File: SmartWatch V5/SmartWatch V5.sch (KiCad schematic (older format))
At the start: 60 parts, among them J1 10118192-0001LF, J10 TestPad, J2 , J7 TestPad, J8 TestPad, J9 TestPad, Q1 FDN340P, Q2 MMBT3904, Q3 MMBT3904, SW1 EVQ-P7J01P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

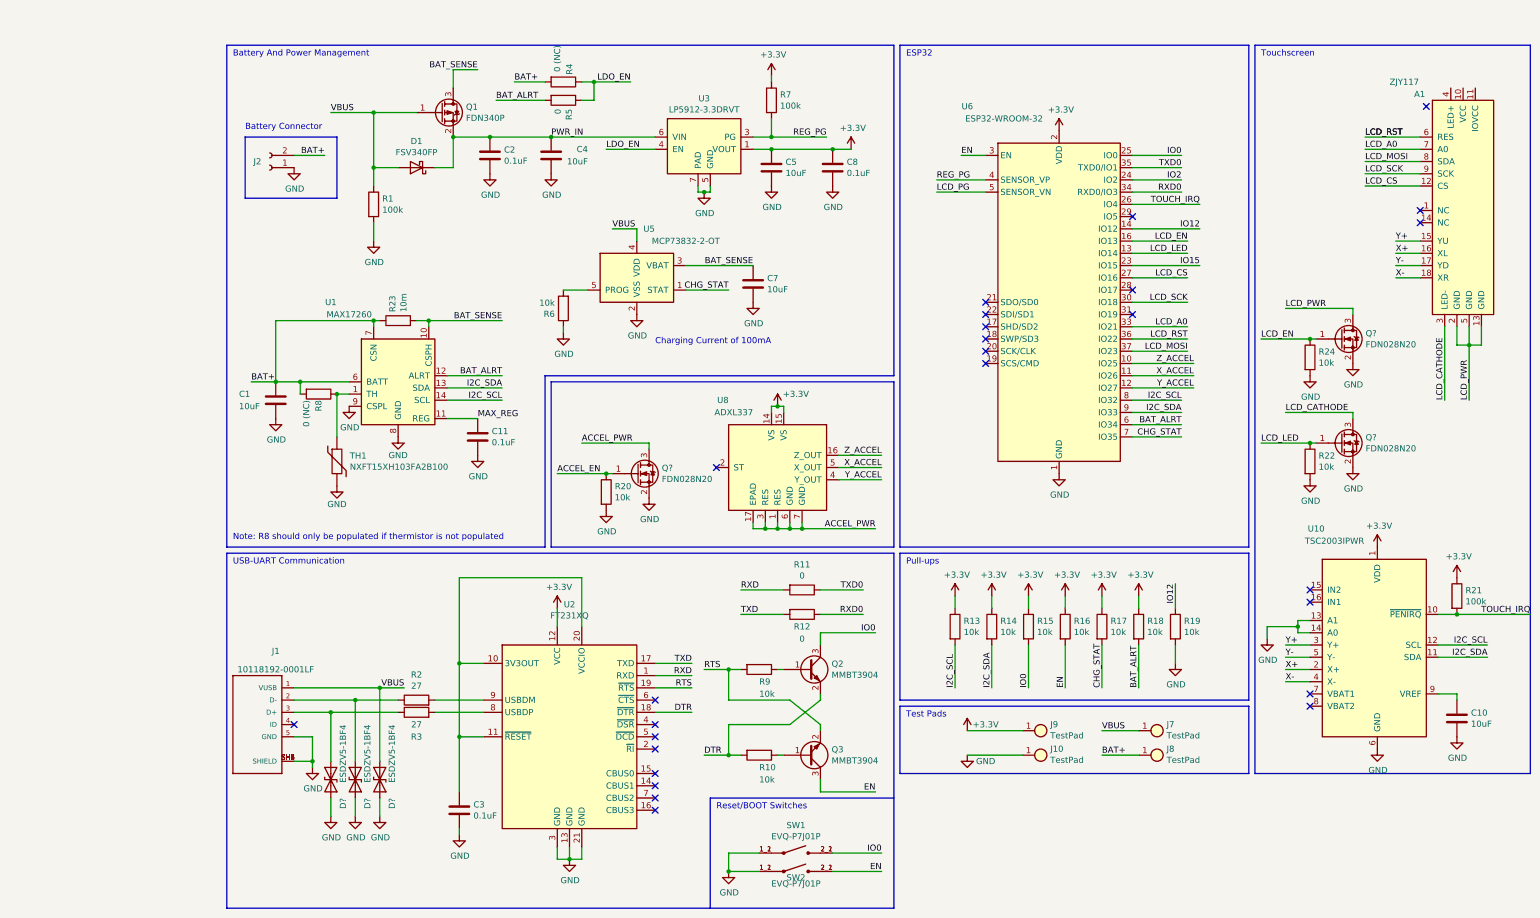
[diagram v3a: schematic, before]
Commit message: Added footprint for Thermistor
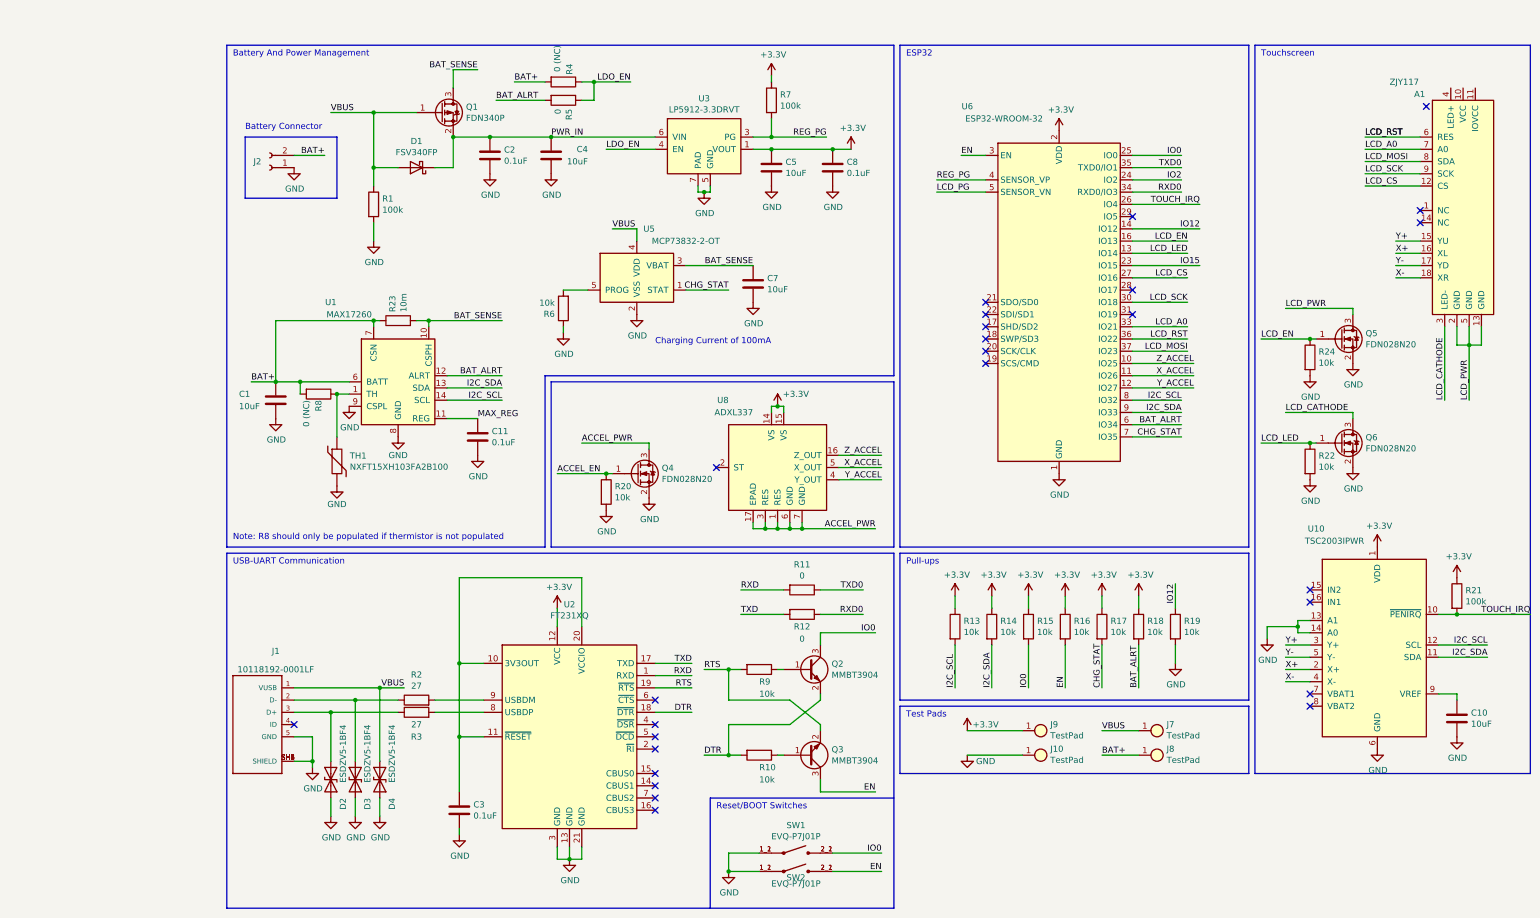
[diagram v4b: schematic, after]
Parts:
- TH1: footprint (none) -> Connector_PinHeader_1.00mm:PinHeader_1x02_P1.00mm_Vertical
- gave numbers to parts that had none: 6
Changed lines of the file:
@@
 F 0 "TH1" H 1555 3996 50  0000 L CNN
 F 1 "NXFT15XH103FA2B100" H 1555 3905 50  0000 L CNN
-F 2 "" H 1450 3950 50  0001 C CNN
+F 2 "Connector_PinHeader_1.00mm:PinHeader_1x02_P1.00mm_Vertical" H 1450 3950 50  0001 C CNN
 F 3 "https://www.murata.com/~/media/webrenewal/support/library/catalog/products/thermistor/ntc/r44e.ashx?la=en-us" H 1450 3950 50  0001 C CNN
 F 4 "490-5630-ND" H 1450 3950 50  0001 C CNN "digikey"
@@
 	3200 3300 6000 3300
 $Comp
-L Device:Q_NMOS_GSD Q?
+L Device:Q_NMOS_GSD Q6
 U 1 1 5F89B605
 P 9650 3800
-F 0 "Q?" H 9854 3846 50  0000 L CNN
+F 0 "Q6" H 9854 3846 50  0000 L CNN
 F 1 "FDN028N20" H 9854 3755 50  0000 L CNN
 F 2 "Package_TO_SOT_SMD:SOT-23" H 9850 3900 50  0001 C CNN
@@
 $EndComp
 $Comp
-L Device:Q_NMOS_GSD Q?
+L Device:Q_NMOS_GSD Q5
 U 1 1 5F89CF73
 P 9650 2950
-F 0 "Q?" H 9854 2996 50  0000 L CNN
+F 0 "Q5" H 9854 2996 50  0000 L CNN
 F 1 "FDN028N20" H 9854 2905 50  0000 L CNN
 F 2 "Package_TO_SOT_SMD:SOT-23" H 9850 3050 50  0001 C CNN
@@
 $EndComp
 $Comp
-L Device:Q_NMOS_GSD Q?
+L Device:Q_NMOS_GSD Q4
 U 1 1 5F89D454
 P 3900 4050
-F 0 "Q?" H 4104 4096 50  0000 L CNN
+F 0 "Q4" H 4104 4096 50  0000 L CNN
 F 1 "FDN028N20" H 4104 4005 50  0000 L CNN
 F 2 "Package_TO_SOT_SMD:SOT-23" H 4100 4150 50  0001 C CNN
@@
 	8950 550  8950 6500
 $Comp
-L Device:D_TVS D?
+L Device:D_TVS D2
 U 1 1 5F8FA488
 P 1400 6550
-F 0 "D?" H 1550 6650 50  0000 L CNN
+F 0 "D2" H 1550 6650 50  0000 L CNN
 F 1 "ESDZV5-1BF4" H 950 6650 50  0000 L CNN
 F 2 "Diode_SMD:D_0201_0603Metric" H 1400 6550 50  0001 C CNN
@@
 	1100 6000 1400 6000
 $Comp
-L Device:D_TVS D?
+L Device:D_TVS D3
 U 1 1 5F945157
 P 1600 6550
-F 0 "D?" H 1750 6650 50  0000 L CNN
+F 0 "D3" H 1750 6650 50  0000 L CNN
 F 1 "ESDZV5-1BF4" H 1150 6650 50  0000 L CNN
 F 2 "Diode_SMD:D_0201_0603Metric" H 1600 6550 50  0001 C CNN
@@
 $EndComp
 $Comp
-L power:GND #PWR?
+L power:GND #PWR0125
 U 1 1 5F945F46
 P 1400 6850
-F 0 "#PWR?" H 1400 6600 50  0001 C CNN
+F 0 "#PWR0125" H 1400 6600 50  0001 C CNN
 F 1 "GND" H 1405 6677 50  0000 C CNN
 F 2 "" H 1400 6850 50  0001 C CNN
@@
 $EndComp
 $Comp
-L power:GND #PWR?
+L power:GND #PWR0126
 U 1 1 5F946231
 P 1600 6850
-F 0 "#PWR?" H 1600 6600 50  0001 C CNN
+F 0 "#PWR0126" H 1600 6600 50  0001 C CNN
 F 1 "GND" H 1605 6677 50  0000 C CNN
 F 2 "" H 1600 6850 50  0001 C CNN
@@
 	1100 5900 1600 5900
 $Comp
-L Device:D_TVS D?
+L Device:D_TVS D4
 U 1 1 5FA53832
 P 1800 6550
-F 0 "D?" H 1950 6650 50  0000 L CNN
+F 0 "D4" H 1950 6650 50  0000 L CNN
 F 1 "ESDZV5-1BF4" H 1350 6650 50  0000 L CNN
 F 2 "Diode_SMD:D_0201_0603Metric" H 1800 6550 50  0001 C CNN
@@
 $EndComp
 $Comp
-L power:GND #PWR?
+L power:GND #PWR0127
 U 1 1 5FA53838
 P 1800 6850
-F 0 "#PWR?" H 1800 6600 50  0001 C CNN
+F 0 "#PWR0127" H 1800 6600 50  0001 C CNN
 F 1 "GND" H 1805 6677 50  0000 C CNN
 F 2 "" H 1800 6850 50  0001 C CNN

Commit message: Began 4 Layer Layout
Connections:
- net +3V3: now also A1.10 (VCC), A1.11 (IOVCC), A1.4 (LED+)
- net IO15: no longer names the net of U6.23 (IO15)
- net IO2: no longer names the net of U6.24 (IO2)
- net LCD_PG: no longer names the net of U6.5 (SENSOR_VN)
- no-connect marks 26 -> 29
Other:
- note added: "Selected Battery - https://www.digikey.com/product-detail/en/adafruit-industries-llc/3898/1528-2731-ND/9685336 (digikey part number: 1528-2731-ND)"
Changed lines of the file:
@@
 Text Label 3650 1400 0    50   ~ 0
 LDO_EN
-Text Label 6350 1750 0    50   ~ 0
-LCD_PG
-Wire Wire Line
-	6350 1750 6750 1750
 Wire Wire Line
 	4400 1750 4400 1700
@@
 Text Label 8500 1850 2    50   ~ 0
 TOUCH_IRQ
-Text Label 8350 1650 2    50   ~ 0
-IO2
 $Comp
 L Device:R R19
@@
 Wire Wire Line
 	8300 5600 8300 5450
-Wire Wire Line
-	7950 1650 8350 1650
 Wire Bus Line
 	8900 4650 8900 550
@@
 Wire Bus Line
 	11200 550  11200 6500
-Text Label 8500 2350 2    50   ~ 0
-IO15
 $Comp
 L CustomParts:TSC2003IPWR U10
@@
 Wire Bus Line
 	550  4700 550  7600
-Wire Wire Line
-	7950 2350 8500 2350
 Text Label 2900 850  0    50   ~ 0
 BAT+
-Text Label 10100 2150 0    50   ~ 0
-Y+
-Wire Wire Line
-	10100 2150 10300 2150
-Text Label 10100 2250 0    50   ~ 0
-X+
-Wire Wire Line
-	10100 2250 10300 2250
-Text Label 10100 2350 0    50   ~ 0
-Y-
-Wire Wire Line
-	10100 2350 10300 2350
-Text Label 10100 2450 0    50   ~ 0
-X-
-Wire Wire Line
-	10100 2450 10300 2450
 Wire Wire Line
 	8400 2450 7950 2450
@@
 Wire Wire Line
 	7950 2150 8400 2150
-NoConn ~ 10350 1050
 Wire Wire Line
 	10500 2850 10500 3450
@@
 Wire Wire Line
 	1800 5800 2000 5800
+Wire Wire Line
+	10100 2450 10300 2450
+Text Label 10100 2450 0    50   ~ 0
+X-
+Wire Wire Line
+	10100 2350 10300 2350
+Text Label 10100 2350 0    50   ~ 0
+Y-
+Wire Wire Line
+	10100 2250 10300 2250
+Text Label 10100 2250 0    50   ~ 0
+X+
+Wire Wire Line
+	10100 2150 10300 2150
+Text Label 10100 2150 0    50   ~ 0
+Y+
+NoConn ~ 7950 2350
+NoConn ~ 7950 1650
+$Comp
+L power:+3.3V #PWR0128
+U 1 1 5FB2118B
+P 10650 800
+F 0 "#PWR0128" H 10650 650 50  0001 C CNN
+F 1 "+3.3V" H 10665 973 50  0000 C CNN
+F 2 "" H 10650 800 50  0001 C CNN
+F 3 "" H 10650 800 50  0001 C CNN
+	1    10650 800
+	1    0    0    -1
+$EndComp
+Wire Wire Line
+	10550 900  10550 800
+Wire Wire Line
+	10550 800  10650 800
+Wire Wire Line
+	10750 800  10750 900
+Connection ~ 10650 800
+Wire Wire Line
+	10650 800  10750 800
+Wire Wire Line
+	10650 900  10650 800
+NoConn ~ 6750 1750
+NoConn ~ -1200 1350
+Text Notes 600  350  0    50   ~ 0
+Selected Battery - https://www.digikey.com/product-detail/en/adafruit-industries-llc/3898/1528-2731-ND/9685336 (digikey part number: 1528-2731-ND)
 $EndSCHEMATC

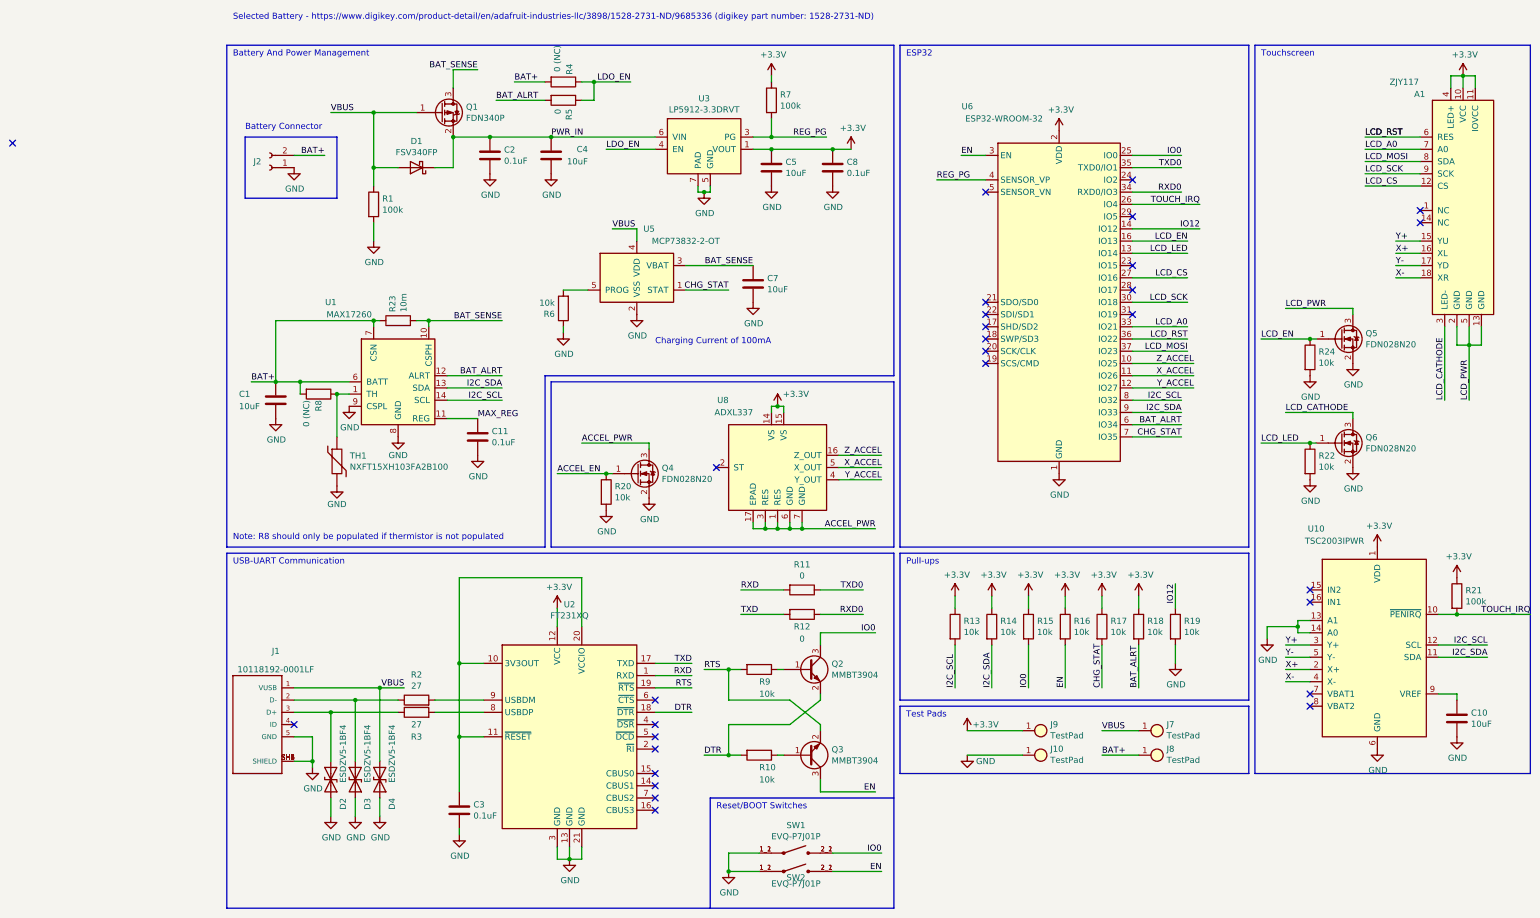
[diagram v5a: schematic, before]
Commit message: Removed 0 ohm jumpers on UART connection
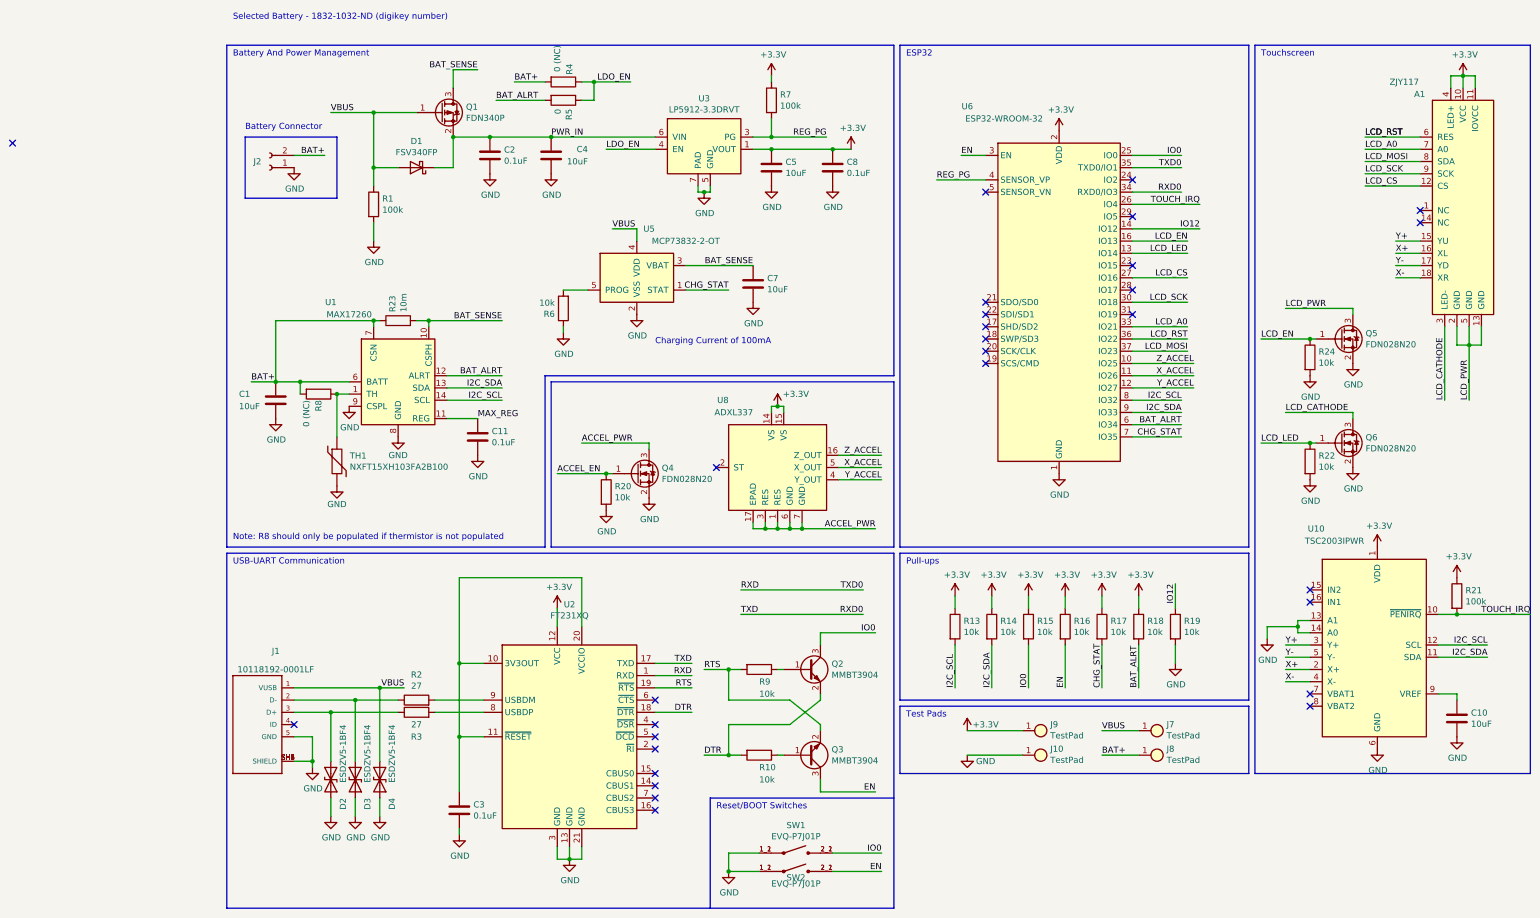
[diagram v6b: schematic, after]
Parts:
- removed R11, R12: 0, Resistor_SMD:R_0603_1608Metric, symbol Device:R
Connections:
- net TXD is gone; now on net RXD0: U2.17 (TXD)
- net TXD0 is gone; now on net RXD: U6.35 (TXD0/IO1)
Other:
- note added: "Selected Battery - 1832-1032-ND (digikey number)"
- note removed: "Selected Battery - https://www.digikey.com/product-detail/en/adafruit-industries-llc/3898/1528-2731-ND/9685336 (digikey part number: 1528-2731-ND)"
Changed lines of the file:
@@
 NoConn ~ 6750 3050
 NoConn ~ 6750 3150
-$Comp
-L Device:R R11
-U 1 1 5E6E7602
-P 5250 5000
-F 0 "R11" V 5043 5000 50  0000 C CNN
-F 1 "0" V 5134 5000 50  0000 C CNN
-F 2 "Resistor_SMD:R_0603_1608Metric" V 5180 5000 50  0001 C CNN
-F 3 "~" H 5250 5000 50  0001 C CNN
-F 4 "RMCF0805ZT0R00CT-ND" V 5250 5000 50  0001 C CNN "digikey"
-	1    5250 5000
-	0    1    1    0
-$EndComp
-$Comp
-L Device:R R12
-U 1 1 5E6E7B1F
-P 5250 5200
-F 0 "R12" V 5350 5200 50  0000 C CNN
-F 1 "0" V 5450 5200 50  0000 C CNN
-F 2 "Resistor_SMD:R_0603_1608Metric" V 5180 5200 50  0001 C CNN
-F 3 "~" H 5250 5200 50  0001 C CNN
-F 4 "RMCF0805ZT0R00CT-ND" V 5250 5200 50  0001 C CNN "digikey"
-	1    5250 5200
-	0    1    1    0
-$EndComp
-Wire Wire Line
-	4750 5000 5100 5000
-Wire Wire Line
-	4750 5200 5100 5200
-Wire Wire Line
-	5400 5200 5750 5200
-Wire Wire Line
-	5400 5000 5750 5000
 Text Label 4750 5000 0    50   ~ 0
 RXD
@@
 NoConn ~ -1200 1350
 Text Notes 600  350  0    50   ~ 0
-Selected Battery - https://www.digikey.com/product-detail/en/adafruit-industries-llc/3898/1528-2731-ND/9685336 (digikey part number: 1528-2731-ND)
+Selected Battery - 1832-1032-ND (digikey number)
+Wire Wire Line
+	4750 5000 5750 5000
+Wire Wire Line
+	4750 5200 5750 5200
 $EndSCHEMATC

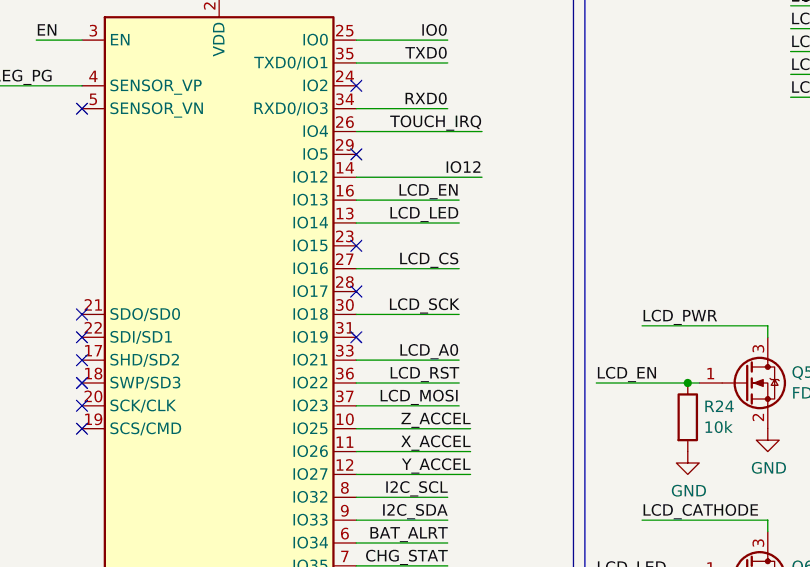
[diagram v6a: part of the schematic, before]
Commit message: Connected ACCEL_EN to ESP32
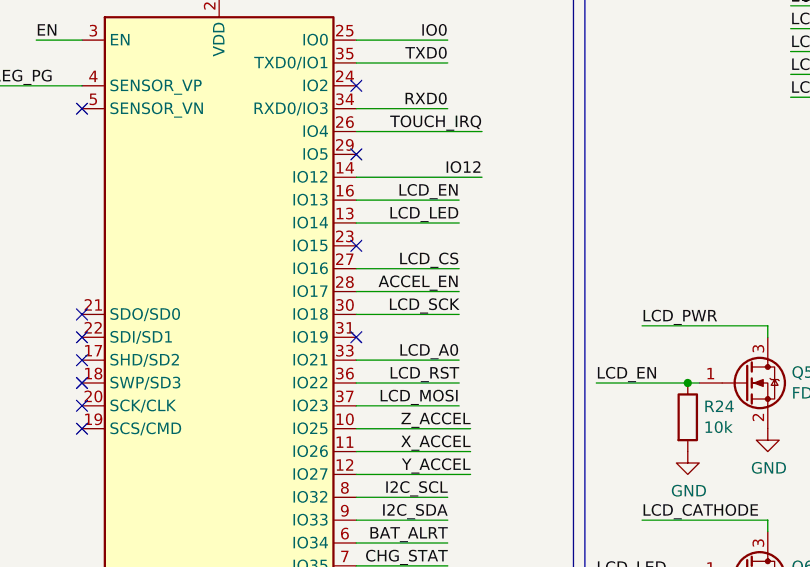
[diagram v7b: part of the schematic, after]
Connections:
- net ACCEL_EN: now also U6.28 (IO17)
- no-connect marks 29 -> 28
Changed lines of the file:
@@
 CHG_STAT
-Wire Wire Line
-	4300 2550 4650 2550
 Wire Wire Line
 	3300 2900 3300 2850
@@
 	3650 4050 3700 4050
 Wire Wire Line
-	3250 4050 3650 4050
-Wire Wire Line
 	4000 3850 4000 3800
 Wire Wire Line
@@
 NoConn ~ 4050 6800
 NoConn ~ 7950 1950
-NoConn ~ 7950 2550
 NoConn ~ 7950 2750
 $Comp
@@
 Wire Wire Line
 	4750 5200 5750 5200
+Wire Wire Line
+	3250 4050 3650 4050
+Wire Wire Line
+	4300 2550 4650 2550
+Text Label 8400 2550 2    50   ~ 0
+ACCEL_EN
+Wire Wire Line
+	7950 2550 8400 2550
 $EndSCHEMATC

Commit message: Layout Work on Rev 5
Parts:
- removed J7: TestPad, CustomFootprints:TESTPAD, symbol CustomParts:TestPad
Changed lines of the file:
@@
-	1    0    0    -1
-$EndComp
-$Comp
-L CustomParts:TestPad J7
-U 1 1 5E8B0641
-P 8000 6150
-F 0 "J7" H 8228 6201 50  0000 L CNN
-F 1 "TestPad" H 8228 6110 50  0000 L CNN
-F 2 "CustomFootprints:TESTPAD" H 8100 6250 50  0001 C CNN
-F 3 "" H 8100 6250 50  0001 C CNN
-	1    8000 6150
 	1    0    0    -1
 $EndComp
@@
 Wire Wire Line
 	7050 6150 6600 6150
-Text Label 7700 6150 0    50   ~ 0
-VBUS
 $Comp
 L power:GND #PWR0112
@@
 	6000 4700 6000 7600
 Wire Wire Line
-	7700 6150 8000 6150
-Wire Wire Line
 	7700 6350 8000 6350
